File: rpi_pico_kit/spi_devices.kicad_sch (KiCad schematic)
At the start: 32 parts, among them J12 Conn_01x08_Male, J13 Conn_01x08_Male, J14 Conn_01x08_Male, J6 Micro_SD_Card_Det, SW10 SW_Push, SW7 SW_Push, SW8 SW_Push, SW9 SW_Push, U6 MCP23S08-xSO

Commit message: added MPNs for capacitors
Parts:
- C21, C22: Manufacturer Part Number (none) -> C0805C104M3RAC7800; Supplier (none) -> Digikey; Supplier Part URL (none) -> https://www.digikey.cz/en/products/detail/kemet/C0805C104M3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
- SW10, SW7, SW8, SW9: Manufacturer Part Number (none) -> LA215000; Supplier (none) -> Laskakit; Supplier Part URL (none) -> https://www.laskakit.cz/tlacitko-6x6x5mm/
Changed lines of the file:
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@@
+      (effects (font (size 1.27 1.27)) hide)
+    )
+    (property "Manufacturer Part Number" "C0805C104M3RAC7800" (id 4) (at 72.39 35.56 0)
+      (effects (font (size 1.27 1.27)) hide)
+    )
+    (property "Supplier" "Digikey" (id 5) (at 72.39 35.56 0)
+      (effects (font (size 1.27 1.27)) hide)
+    )
+    (property "Supplier Part URL" "https://www.digikey.cz/en/products/detail/kemet/C0805C104M3RAC7800/2211748" (id 6) (at 72.39 35.56 0)
       (effects (font (size 1.27 1.27)) hide)
     )
@@
     )
     (property "Datasheet" "~" (id 3) (at 128.27 38.1 0)
+      (effects (font (size 1.27 1.27)) hide)
+    )
+    (property "Manufacturer Part Number" "LA215000" (id 4) (at 133.35 38.1 0)
+      (effects (font (size 1.27 1.27)) hide)
+    )
+    (property "Supplier" "Laskakit" (id 5) (at 133.35 38.1 0)
+      (effects (font (size 1.27 1.27)) hide)
+    )
+    (property "Supplier Part URL" "https://www.laskakit.cz/tlacitko-6x6x5mm/" (id 6) (at 133.35 38.1 0)
       (effects (font (size 1.27 1.27)) hide)
     )
@@
       (effects (font (size 1.27 1.27)) hide)
     )
+    (property "Manufacturer Part Number" "C0805C104M3RAC7800" (id 4) (at 184.15 110.49 0)
+      (effects (font (size 1.27 1.27)) hide)
+    )
+    (property "Supplier" "Digikey" (id 5) (at 184.15 110.49 0)
+      (effects (font (size 1.27 1.27)) hide)
+    )
+    (property "Supplier Part URL" "https://www.digikey.cz/en/products/detail/kemet/C0805C104M3RAC7800/2211748" (id 6) (at 184.15 110.49 0)
+      (effects (font (size 1.27 1.27)) hide)
+    )
     (pin "1")
     (pin "2")
@@
     )
     (property "Datasheet" "~" (id 3) (at 166.37 38.1 0)
+      (effects (font (size 1.27 1.27)) hide)
+    )
+    (property "Manufacturer Part Number" "LA215000" (id 4) (at 171.45 38.1 0)
+      (effects (font (size 1.27 1.27)) hide)
+    )
+    (property "Supplier" "Laskakit" (id 5) (at 171.45 38.1 0)
+      (effects (font (size 1.27 1.27)) hide)
+    )
+    (property "Supplier Part URL" "https://www.laskakit.cz/tlacitko-6x6x5mm/" (id 6) (at 171.45 38.1 0)
       (effects (font (size 1.27 1.27)) hide)
     )
@@
       (effects (font (size 1.27 1.27)) hide)
     )
+    (property "Manufacturer Part Number" "LA215000" (id 4) (at 146.05 38.1 0)
+      (effects (font (size 1.27 1.27)) hide)
+    )
+    (property "Supplier" "Laskakit" (id 5) (at 146.05 38.1 0)
+      (effects (font (size 1.27 1.27)) hide)
+    )
+    (property "Supplier Part URL" "https://www.laskakit.cz/tlacitko-6x6x5mm/" (id 6) (at 146.05 38.1 0)
+      (effects (font (size 1.27 1.27)) hide)
+    )
     (pin "1")
     (pin "2")
@@
       (effects (font (size 1.27 1.27)) hide)
     )
+    (property "Manufacturer Part Number" "LA215000" (id 4) (at 158.75 38.1 0)
+      (effects (font (size 1.27 1.27)) hide)
+    )
+    (property "Supplier" "Laskakit" (id 5) (at 158.75 38.1 0)
+      (effects (font (size 1.27 1.27)) hide)
+    )
+    (property "Supplier Part URL" "https://www.laskakit.cz/tlacitko-6x6x5mm/" (id 6) (at 158.75 38.1 0)
+      (effects (font (size 1.27 1.27)) hide)
+    )

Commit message: added MPNs for resistors
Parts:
- R65, R66, R67, R68, R69, R70, R71, R72, R73, R74, R75, R76, R77, R94, R95, R96, R97: Manufacturer Part Number (none) -> RC0805FR-071KL; Supplier (none) -> Digikey; Supplier Part URL (none) -> https://www.digikey.cz/en/products/detail/yageo/RC0805FR-07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
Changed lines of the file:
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@@
+      (effects (font (size 1.27 1.27)) hide)
+    )
+    (property "Manufacturer Part Number" "RC0805FR-071KL" (id 4) (at 125.73 142.24 0)
+      (effects (font (size 1.27 1.27)) hide)
+    )
+    (property "Supplier Part URL" "https://www.digikey.cz/en/products/detail/yageo/RC0805FR-071KL/727444" (id 5) (at 125.73 142.24 0)
+      (effects (font (size 1.27 1.27)) hide)
+    )
+    (property "Supplier" "Digikey" (id 6) (at 125.73 142.24 0)
       (effects (font (size 1.27 1.27)) hide)
     )
@@
       (effects (font (size 1.27 1.27)) hide)
     )
+    (property "Manufacturer Part Number" "RC0805FR-071KL" (id 4) (at 125.73 127 0)
+      (effects (font (size 1.27 1.27)) hide)
+    )
+    (property "Supplier Part URL" "https://www.digikey.cz/en/products/detail/yageo/RC0805FR-071KL/727444" (id 5) (at 125.73 127 0)
+      (effects (font (size 1.27 1.27)) hide)
+    )
+    (property "Supplier" "Digikey" (id 6) (at 125.73 127 0)
+      (effects (font (size 1.27 1.27)) hide)
+    )
     (pin "1")
     (pin "2")
@@
     )
     (property "Datasheet" "~" (id 3) (at 146.05 73.66 0)
+      (effects (font (size 1.27 1.27)) hide)
+    )
+    (property "Manufacturer Part Number" "RC0805FR-071KL" (id 4) (at 146.05 73.66 0)
+      (effects (font (size 1.27 1.27)) hide)
+    )
+    (property "Supplier Part URL" "https://www.digikey.cz/en/products/detail/yageo/RC0805FR-071KL/727444" (id 5) (at 146.05 73.66 0)
+      (effects (font (size 1.27 1.27)) hide)
+    )
+    (property "Supplier" "Digikey" (id 6) (at 146.05 73.66 0)
       (effects (font (size 1.27 1.27)) hide)
     )
@@
       (effects (font (size 1.27 1.27)) hide)
     )
+    (property "Manufacturer Part Number" "RC0805FR-071KL" (id 4) (at 123.19 67.31 0)
+      (effects (font (size 1.27 1.27)) hide)
+    )
+    (property "Supplier Part URL" "https://www.digikey.cz/en/products/detail/yageo/RC0805FR-071KL/727444" (id 5) (at 123.19 67.31 0)
+      (effects (font (size 1.27 1.27)) hide)
+    )
+    (property "Supplier" "Digikey" (id 6) (at 123.19 67.31 0)
+      (effects (font (size 1.27 1.27)) hide)
+    )
     (pin "1")
     (pin "2")
@@
       (effects (font (size 1.27 1.27)) hide)
     )
+    (property "Manufacturer Part Number" "RC0805FR-071KL" (id 4) (at 158.75 73.66 0)
+      (effects (font (size 1.27 1.27)) hide)
+    )
+    (property "Supplier Part URL" "https://www.digikey.cz/en/products/detail/yageo/RC0805FR-071KL/727444" (id 5) (at 158.75 73.66 0)
+      (effects (font (size 1.27 1.27)) hide)
+    )
+    (property "Supplier" "Digikey" (id 6) (at 158.75 73.66 0)
+      (effects (font (size 1.27 1.27)) hide)
+    )
     (pin "1")
     (pin "2")
@@
       (effects (font (size 1.27 1.27)) hide)
     )
+    (property "Manufacturer Part Number" "RC0805FR-071KL" (id 4) (at 125.73 137.16 0)
+      (effects (font (size 1.27 1.27)) hide)
+    )
+    (property "Supplier Part URL" "https://www.digikey.cz/en/products/detail/yageo/RC0805FR-071KL/727444" (id 5) (at 125.73 137.16 0)
+      (effects (font (size 1.27 1.27)) hide)
+    )
+    (property "Supplier" "Digikey" (id 6) (at 125.73 137.16 0)
+      (effects (font (size 1.27 1.27)) hide)
+    )
     (pin "1")
     (pin "2")
@@
       (effects (font (size 1.27 1.27)) hide)
     )
+    (property "Manufacturer Part Number" "RC0805FR-071KL" (id 4) (at 123.19 62.23 0)
+      (effects (font (size 1.27 1.27)) hide)
+    )
+    (property "Supplier Part URL" "https://www.digikey.cz/en/products/detail/yageo/RC0805FR-071KL/727444" (id 5) (at 123.19 62.23 0)
+      (effects (font (size 1.27 1.27)) hide)
+    )
+    (property "Supplier" "Digikey" (id 6) (at 123.19 62.23 0)
+      (effects (font (size 1.27 1.27)) hide)
+    )
     (pin "1")
     (pin "2")
@@
       (effects (font (size 1.27 1.27)) hide)
     )
+    (property "Manufacturer Part Number" "RC0805FR-071KL" (id 4) (at 125.73 132.08 0)
+      (effects (font (size 1.27 1.27)) hide)
+    )
+    (property "Supplier Part URL" "https://www.digikey.cz/en/products/detail/yageo/RC0805FR-071KL/727444" (id 5) (at 125.73 132.08 0)
+      (effects (font (size 1.27 1.27)) hide)
+    )
+    (property "Supplier" "Digikey" (id 6) (at 125.73 132.08 0)
+      (effects (font (size 1.27 1.27)) hide)
+    )
     (pin "1")
     (pin "2")
@@
       (effects (font (size 1.27 1.27)) hide)
     )
+    (property "Manufacturer Part Number" "RC0805FR-071KL" (id 4) (at 87.63 73.66 0)
+      (effects (font (size 1.27 1.27)) hide)
+    )
+    (property "Supplier Part URL" "https://www.digikey.cz/en/products/detail/yageo/RC0805FR-071KL/727444" (id 5) (at 87.63 73.66 0)
+      (effects (font (size 1.27 1.27)) hide)
+    )
+    (property "Supplier" "Digikey" (id 6) (at 87.63 73.66 0)
+      (effects (font (size 1.27 1.27)) hide)
+    )
     (pin "1")
     (pin "2")
@@
       (effects (font (size 1.27 1.27)) hide)
     )
+    (property "Manufacturer Part Number" "RC0805FR-071KL" (id 4) (at 133.35 73.66 0)
+      (effects (font (size 1.27 1.27)) hide)
+    )
+    (property "Supplier Part URL" "https://www.digikey.cz/en/products/detail/yageo/RC0805FR-071KL/727444" (id 5) (at 133.35 73.66 0)
+      (effects (font (size 1.27 1.27)) hide)
+    )
+    (property "Supplier" "Digikey" (id 6) (at 133.35 73.66 0)
+      (effects (font (size 1.27 1.27)) hide)
+    )
     (pin "1")
     (pin "2")
@@
     )
     (property "Datasheet" "~" (id 3) (at 114.3 73.66 0)
+      (effects (font (size 1.27 1.27)) hide)
+    )
+    (property "Manufacturer Part Number" "RC0805FR-071KL" (id 4) (at 114.3 73.66 0)
+      (effects (font (size 1.27 1.27)) hide)
+    )
+    (property "Supplier Part URL" "https://www.digikey.cz/en/products/detail/yageo/RC0805FR-071KL/727444" (id 5) (at 114.3 73.66 0)
+      (effects (font (size 1.27 1.27)) hide)
+    )
+    (property "Supplier" "Digikey" (id 6) (at 114.3 73.66 0)
       (effects (font (size 1.27 1.27)) hide)
     )
@@
       (effects (font (size 1.27 1.27)) hide)
     )
+    (property "Manufacturer Part Number" "RC0805FR-071KL" (id 4) (at 171.45 73.66 0)
+      (effects (font (size 1.27 1.27)) hide)
+    )
+    (property "Supplier Part URL" "https://www.digikey.cz/en/products/detail/yageo/RC0805FR-071KL/727444" (id 5) (at 171.45 73.66 0)
+      (effects (font (size 1.27 1.27)) hide)
+    )
+    (property "Supplier" "Digikey" (id 6) (at 171.45 73.66 0)
+      (effects (font (size 1.27 1.27)) hide)
+    )
     (pin "1")
     (pin "2")
@@
       (effects (font (size 1.27 1.27)) hide)
     )
+    (property "Manufacturer Part Number" "RC0805FR-071KL" (id 4) (at 125.73 121.92 0)
+      (effects (font (size 1.27 1.27)) hide)
+    )
+    (property "Supplier Part URL" "https://www.digikey.cz/en/products/detail/yageo/RC0805FR-071KL/727444" (id 5) (at 125.73 121.92 0)
+      (effects (font (size 1.27 1.27)) hide)
+    )
+    (property "Supplier" "Digikey" (id 6) (at 125.73 121.92 0)
+      (effects (font (size 1.27 1.27)) hide)
+    )
     (pin "1")
     (pin "2")
@@
     )
     (property "Datasheet" "~" (id 3) (at 105.41 73.66 0)
+      (effects (font (size 1.27 1.27)) hide)
+    )
+    (property "Manufacturer Part Number" "RC0805FR-071KL" (id 4) (at 105.41 73.66 0)
+      (effects (font (size 1.27 1.27)) hide)
+    )
+    (property "Supplier Part URL" "https://www.digikey.cz/en/products/detail/yageo/RC0805FR-071KL/727444" (id 5) (at 105.41 73.66 0)
+      (effects (font (size 1.27 1.27)) hide)
+    )
+    (property "Supplier" "Digikey" (id 6) (at 105.41 73.66 0)
       (effects (font (size 1.27 1.27)) hide)
     )
@@
       (effects (font (size 1.27 1.27)) hide)
     )
+    (property "Manufacturer Part Number" "RC0805FR-071KL" (id 4) (at 96.52 73.66 0)
+      (effects (font (size 1.27 1.27)) hide)
+    )
+    (property "Supplier Part URL" "https://www.digikey.cz/en/products/detail/yageo/RC0805FR-071KL/727444" (id 5) (at 96.52 73.66 0)
+      (effects (font (size 1.27 1.27)) hide)
+    )
+    (property "Supplier" "Digikey" (id 6) (at 96.52 73.66 0)
+      (effects (font (size 1.27 1.27)) hide)
+    )
     (pin "1")
     (pin "2")
@@
     )
     (property "Datasheet" "~" (id 3) (at 123.19 59.69 0)
+      (effects (font (size 1.27 1.27)) hide)
+    )
+    (property "Manufacturer Part Number" "RC0805FR-071KL" (id 4) (at 123.19 59.69 0)
+      (effects (font (size 1.27 1.27)) hide)
+    )
+    (property "Supplier Part URL" "https://www.digikey.cz/en/products/detail/yageo/RC0805FR-071KL/727444" (id 5) (at 123.19 59.69 0)
+      (effects (font (size 1.27 1.27)) hide)
+    )
+    (property "Supplier" "Digikey" (id 6) (at 123.19 59.69 0)
       (effects (font (size 1.27 1.27)) hide)
     )
@@
       (effects (font (size 1.27 1.27)) hide)
     )
+    (property "Manufacturer Part Number" "RC0805FR-071KL" (id 4) (at 123.19 64.77 0)
+      (effects (font (size 1.27 1.27)) hide)
+    )
+    (property "Supplier Part URL" "https://www.digikey.cz/en/products/detail/yageo/RC0805FR-071KL/727444" (id 5) (at 123.19 64.77 0)
+      (effects (font (size 1.27 1.27)) hide)
+    )
+    (property "Supplier" "Digikey" (id 6) (at 123.19 64.77 0)
+      (effects (font (size 1.27 1.27)) hide)
+    )

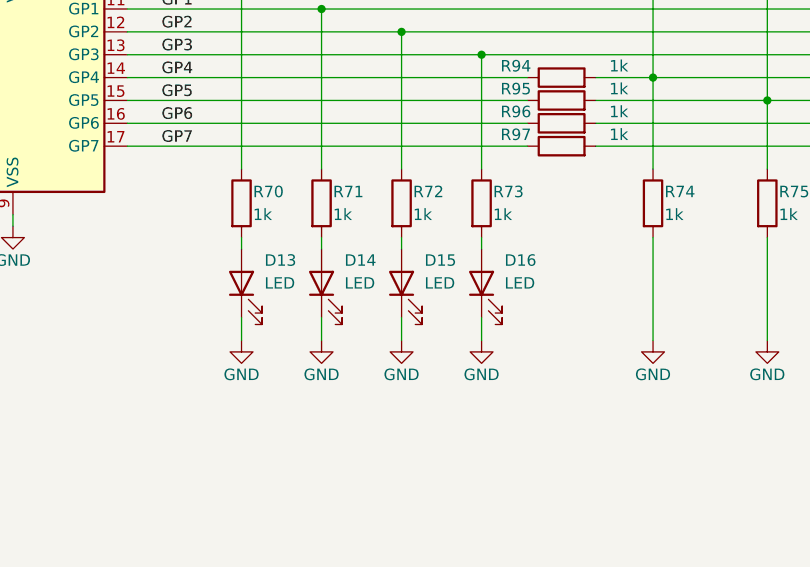
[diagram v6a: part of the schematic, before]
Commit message: added another MPNs, edited color of LEDs
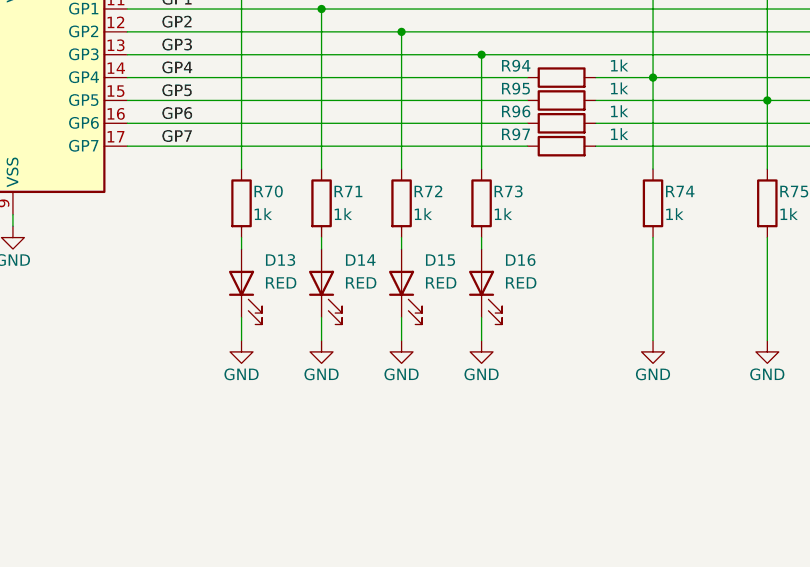
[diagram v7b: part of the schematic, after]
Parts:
- D13, D14, D15, D16: value LED -> RED
- J12, J13, J14: Manufacturer Part Number (none) -> PinHeader_1x08
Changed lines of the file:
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@@
       (effects (font (size 1.27 1.27)) (justify right))
     )
-    (property "Value" "LED" (id 1) (at 99.06 82.55 90)
+    (property "Value" "RED" (id 1) (at 99.06 82.55 90)
       (effects (font (size 1.27 1.27)) (justify right))
     )
@@
       (effects (font (size 1.27 1.27)) (justify right))
     )
-    (property "Value" "LED" (id 1) (at 116.84 82.55 90)
+    (property "Value" "RED" (id 1) (at 116.84 82.55 90)
       (effects (font (size 1.27 1.27)) (justify right))
     )
@@
     )
     (property "Datasheet" "~" (id 3) (at 232.41 57.15 0)
+      (effects (font (size 1.27 1.27)) hide)
+    )
+    (property "Manufacturer Part Number" "PinHeader_1x08" (id 4) (at 232.41 57.15 0)
       (effects (font (size 1.27 1.27)) hide)
     )
@@
       (effects (font (size 1.27 1.27)) (justify right))
     )
-    (property "Value" "LED" (id 1) (at 90.17 82.55 90)
+    (property "Value" "RED" (id 1) (at 90.17 82.55 90)
       (effects (font (size 1.27 1.27)) (justify right))
     )
@@
       (effects (font (size 1.27 1.27)) hide)
     )
+    (property "Manufacturer Part Number" "PinHeader_1x08" (id 4) (at 184.15 57.15 0)
+      (effects (font (size 1.27 1.27)) hide)
+    )
     (pin "1")
     (pin "2")
@@
       (effects (font (size 1.27 1.27)) hide)
     )
+    (property "Manufacturer Part Number" "PinHeader_1x08" (id 4) (at 208.28 57.15 0)
+      (effects (font (size 1.27 1.27)) hide)
+    )
     (pin "1")
     (pin "2")
@@
       (effects (font (size 1.27 1.27)) (justify right))
     )
-    (property "Value" "LED" (id 1) (at 107.95 82.55 90)
-      (effects (font (size 1.27 1.27)) (justify right))
-    )
+    (property "Value" "RED" (id 1) (at 107.95 82.55 90)
+      (effects (font (size 1.27 1.27)) (justify right))
+    )

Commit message: changed name of LEDs from D to LED
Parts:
- renumbered D14 to LED10, D15 to LED11, D16 to LED12, D13 to LED9
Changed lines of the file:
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@@
   (symbol (lib_id "Device:LED") (at 96.52 82.55 90) (unit 1)
     (in_bom yes) (on_board yes)
-    (property "Reference" "D14" (id 0) (at 99.06 80.01 90)
+    (property "Reference" "LED10" (id 0) (at 99.06 80.01 90)
       (effects (font (size 1.27 1.27)) (justify right))
     )
@@
   (symbol (lib_id "Device:LED") (at 114.3 82.55 90) (unit 1)
     (in_bom yes) (on_board yes)
-    (property "Reference" "D16" (id 0) (at 116.84 80.01 90)
+    (property "Reference" "LED12" (id 0) (at 116.84 80.01 90)
       (effects (font (size 1.27 1.27)) (justify right))
     )
@@
   (symbol (lib_id "Device:LED") (at 87.63 82.55 90) (unit 1)
     (in_bom yes) (on_board yes)
-    (property "Reference" "D13" (id 0) (at 90.17 80.01 90)
+    (property "Reference" "LED9" (id 0) (at 90.17 80.01 90)
       (effects (font (size 1.27 1.27)) (justify right))
     )
@@
   (symbol (lib_id "Device:LED") (at 105.41 82.55 90) (unit 1)
     (in_bom yes) (on_board yes)
-    (property "Reference" "D15" (id 0) (at 107.95 80.01 90)
+    (property "Reference" "LED11" (id 0) (at 107.95 80.01 90)
       (effects (font (size 1.27 1.27)) (justify right))
     )
